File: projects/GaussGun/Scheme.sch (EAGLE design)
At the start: 25 parts, among them IC1 NE555N, T1 TIC126, T2 TIC126, T3 2N2222

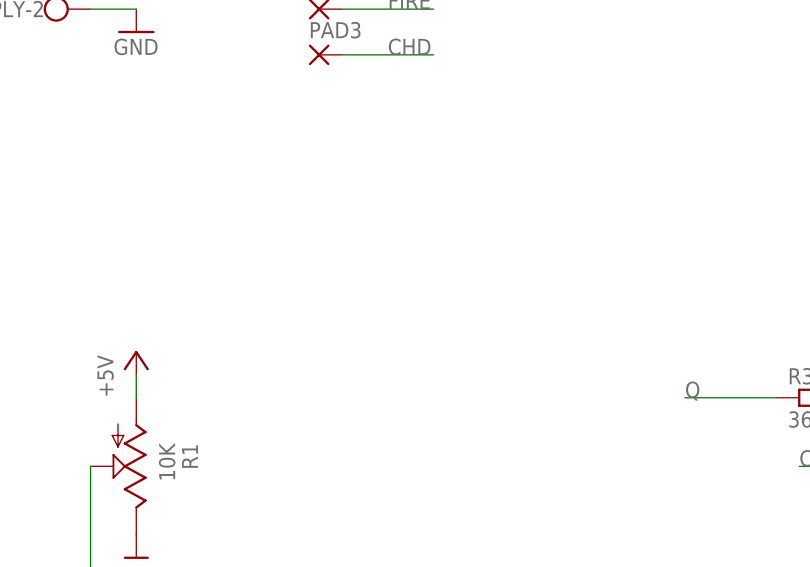
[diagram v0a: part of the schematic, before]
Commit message: Added 5v supply
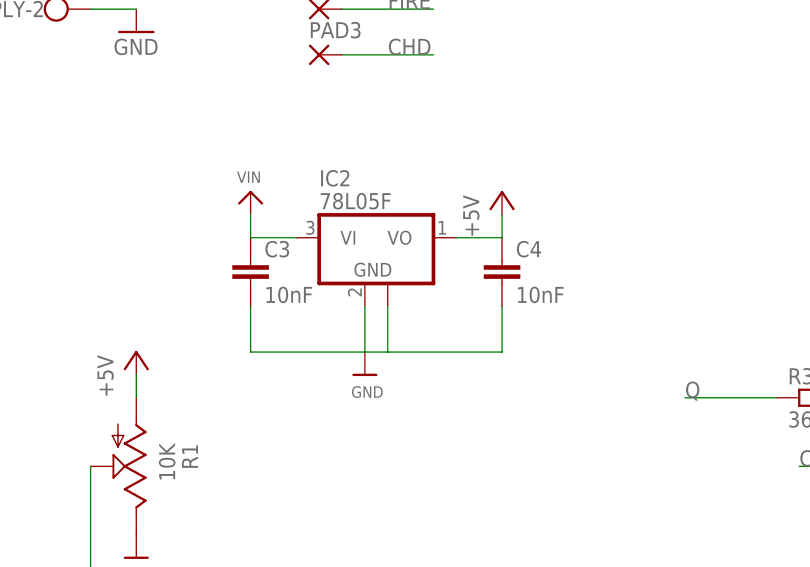
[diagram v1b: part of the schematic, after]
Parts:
- added C3, C4: 10nF, rcl:C-EU025-024X044
- added IC2: 78L05F, linear:78L05F
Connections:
- net +5V: now also C4.1, IC2.VO
- net GND: now also C3.2, C4.2, IC2.GND, IC2.GND@1
- net VIN: now also C3.1, IC2.VI
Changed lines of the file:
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@@
 <part name="LED1" library="adafruit" deviceset="LED" device="3MM"/>
 <part name="R6" library="rcl" deviceset="R-EU_" device="R1206"/>
+<part name="IC2" library="linear" deviceset="78L*" device="F" technology="05"/>
+<part name="P+5" library="supply1" deviceset="+5V" device=""/>
+<part name="U$8" library="microbuilder" deviceset="VIN" device=""/>
+<part name="U$9" library="microbuilder" deviceset="GND" device=""/>
+<part name="C3" library="rcl" deviceset="C-EU" device="025-024X044" value="10nF"/>
+<part name="C4" library="rcl" deviceset="C-EU" device="025-024X044" value="10nF"/>
 </parts>
 <sheets>
@@
 <instance part="LED1" gate="G$1" x="127" y="101.6"/>
 <instance part="R6" gate="G$1" x="127" y="91.44" rot="R90"/>
+<instance part="IC2" gate="G$1" x="27.94" y="106.68"/>
+<instance part="P+5" gate="1" x="43.18" y="111.76"/>
+<instance part="U$8" gate="G$1" x="15.24" y="111.76"/>
+<instance part="U$9" gate="G$1" x="27.94" y="91.44"/>
+<instance part="C3" gate="G$1" x="15.24" y="104.14"/>
+<instance part="C4" gate="G$1" x="43.18" y="104.14"/>
 </instances>
 <busses>
@@
 <wire x1="127" y1="76.2" x2="127" y2="55.88" width="0.1524" layer="91"/>
 </segment>
+<segment>
+<pinref part="IC2" gate="G$1" pin="GND"/>
+<pinref part="U$9" gate="G$1" pin="GND"/>
+<wire x1="27.94" y1="93.98" x2="27.94" y2="99.06" width="0.1524" layer="91"/>
+<pinref part="C3" gate="G$1" pin="2"/>
+<wire x1="15.24" y1="99.06" x2="15.24" y2="93.98" width="0.1524" layer="91"/>
+<wire x1="15.24" y1="93.98" x2="27.94" y2="93.98" width="0.1524" layer="91"/>
+<pinref part="C4" gate="G$1" pin="2"/>
+<wire x1="43.18" y1="99.06" x2="43.18" y2="93.98" width="0.1524" layer="91"/>
+<wire x1="43.18" y1="93.98" x2="30.48" y2="93.98" width="0.1524" layer="91"/>
+<pinref part="IC2" gate="G$1" pin="GND@1"/>
+<wire x1="30.48" y1="93.98" x2="27.94" y2="93.98" width="0.1524" layer="91"/>
+<wire x1="30.48" y1="99.06" x2="30.48" y2="93.98" width="0.1524" layer="91"/>
+</segment>
 </net>
 <net name="N$2" class="0">
@@
 <pinref part="P+4" gate="1" pin="+5V"/>
 </segment>
+<segment>
+<pinref part="IC2" gate="G$1" pin="VO"/>
+<pinref part="C4" gate="G$1" pin="1"/>
+<wire x1="38.1" y1="106.68" x2="43.18" y2="106.68" width="0.1524" layer="91"/>
+<pinref part="P+5" gate="1" pin="+5V"/>
+<wire x1="43.18" y1="109.22" x2="43.18" y2="106.68" width="0.1524" layer="91"/>
+</segment>
 </net>
 <net name="VIN" class="0">
@@
 <wire x1="99.06" y1="139.7" x2="99.06" y2="134.62" width="0.1524" layer="91"/>
 </segment>
-</net>
+<segment>
+<pinref part="IC2" gate="G$1" pin="VI"/>
+<pinref part="C3" gate="G$1" pin="1"/>
+<wire x1="20.32" y1="106.68" x2="15.24" y2="106.68" width="0.1524" layer="91"/>
+<pinref part="U$8" gate="G$1" pin="VIN"/>
+<wire x1="15.24" y1="106.68" x2="15.24" y2="109.22" width="0.1524" layer="91"/>
+</segment>
+</net>
